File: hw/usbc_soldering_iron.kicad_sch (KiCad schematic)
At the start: 78 parts, among them J1 USB_C_Receptacle_USB2.0_14P, J10 TIP_L, J11 TIP_H, J12 TIP_K, J13 TIP_L, J14 TIP_H, J15 TIP_K, J16 TIP_L, J2 DBG, J3 LED RING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

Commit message: mosfets and driver
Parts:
- added C29, C30, C31: 100n, Capacitor_SMD:C_0603_1608Metric, symbol Device:C_Small
- added D1: CDBU40-HF, Diode_SMD:D_0603_1608Metric, symbol Diode:CDBU40-HF
- added Q1, Q2: CSD16327Q3, Package_SON:VSON-8_3.3x3.3mm_P0.65mm_NexFET, symbol Transistor_FET:CSD16327Q3
- added R10: 1.5m, Resistor_SMD:R_1206_3216Metric, symbol Device:R_Small
- added R11: 10k, Capacitor_SMD:C_0603_1608Metric, symbol Device:R_Small
- added U10: PLM74502QDDFRQ1, Package_TO_SOT_SMD:SOT-23-8, symbol custom_library:PLM74502QDDFRQ1
- added U8: IRS20752L, Package_TO_SOT_SMD:SOT-23-6, symbol custom_library:IRS20752L
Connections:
- net +3.3V: now also C30.1, D1.2 (A), U8.1 (VCC)
- net GND: now also C30.2, U10.2 (GND), U8.2 (COM)
- net HEATER_ON: now also U8.3 (IN)
- net VBUS: now also U6.4 (IN+), R10.1; no longer C23.1, C25.1, L2.1
- net at U6.5 (IN-): now also C31.1, Q2.5 (D), R10.2, R11.1, U10.5 (VS)
- net at C26.1, C28.1, L2.2: now also Q1.5 (D)
- new net: C31.2, U10.4 (VCAP)
- new net: Q2.4 (G), U10.6 (GATE)
- new net: C23.1, C25.1, L2.1, Q2.1 (S), Q2.2 (S), Q2.3 (S), R11.2, U10.8 (SRC)
- new net: C29.1, D1.1 (K), U8.6 (VB)
- new net: C29.2, Q1.1 (S), Q1.2 (S), Q1.3 (S), U8.4 (VS)
- new net: Q1.4 (G), U8.5 (HO)
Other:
- note removed: "TIP CONTROL"
- moved on the sheet: C14, C23, C25, C26, C28, L2, U6

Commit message: different mosfets
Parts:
- removed C31: 100n, Capacitor_SMD:C_0603_1608Metric, symbol Device:C_Small
- removed Q2: CSD16327Q3, Package_SON:VSON-8_3.3x3.3mm_P0.65mm_NexFET, symbol Transistor_FET:CSD16327Q3
- removed R11: 10k, Capacitor_SMD:C_0603_1608Metric, symbol Device:R_Small
- removed U10: PLM74502QDDFRQ1, Package_TO_SOT_SMD:SOT-23-8, symbol custom_library:PLM74502QDDFRQ1
- added U10: CSD25402Q3A, Package_SON:VSON-8_3.3x3.3mm_P0.65mm_NexFET, symbol Transistor_FET:CSD25402Q3A
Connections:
- net at R10.2, U6.5 (IN-): now also U10.5 (S)
- net at C23.1, C25.1, L2.1: now also U10.1 (D), U10.2 (D), U10.3 (D)

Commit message: work on model
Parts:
- added SW4: SW_Push, symbol Switch:SW_Push
- L1: footprint Inductor_SMD:L_Changjiang_FTC201607S -> Inductor_SMD:L_Changjiang_FTC252012S
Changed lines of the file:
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@@
 			)
 		)
-		(property "Footprint" "Inductor_SMD:L_Changjiang_FTC201607S"
+		(property "Footprint" "Inductor_SMD:L_Changjiang_FTC252012S"
 			(at 152.4 27.94 0)
 			(effects
@@
 					(unit 1)
 				)
+			)
+		)
+	)
+	(symbol
+		(lib_id "Switch:SW_Push")
+		(at 217.17 234.95 0)
+		(unit 1)
+		(exclude_from_sim no)
+		(in_bom yes)
+		(on_board yes)
+		(dnp no)
+		(fields_autoplaced yes)
+		(property "Reference" "SW4"
+			(at 217.17 227.33 0)
+			(effects
+				(font
+					(size 1.27 1.27)
+				)
+			)
+		)
+		(property "Value" "SW_Push"
+			(at 217.17 229.87 0)
+			(effects
+				(font
+					(size 1.27 1.27)
+				)
+			)
+		)
+		(property "Footprint" ""
+			(at 217.17 229.87 0)
+			(effects
+				(font
+					(size 1.27 1.27)
+				)
+				(hide yes)
+			)
+		)
+		(property "Datasheet" "~"
+			(at 217.17 229.87 0)
+			(effects
+				(font
+					(size 1.27 1.27)
+				)
+				(hide yes)
+			)
+		)
+		(property "Description" "Push button switch, generic, two pins"
+			(at 217.17 234.95 0)
+			(effects
+				(font
+					(size 1.27 1.27)
+				)
+				(hide yes)
+			)
+		)
+		(pin "2"
+		)
+		(pin "1"
+		)
+		(instances
+			(project ""
+				(path "/7095b018-eac3-4b01-b374-28e3216c4fd8"
+					(reference "SW4")
+					(unit 1)
+				)

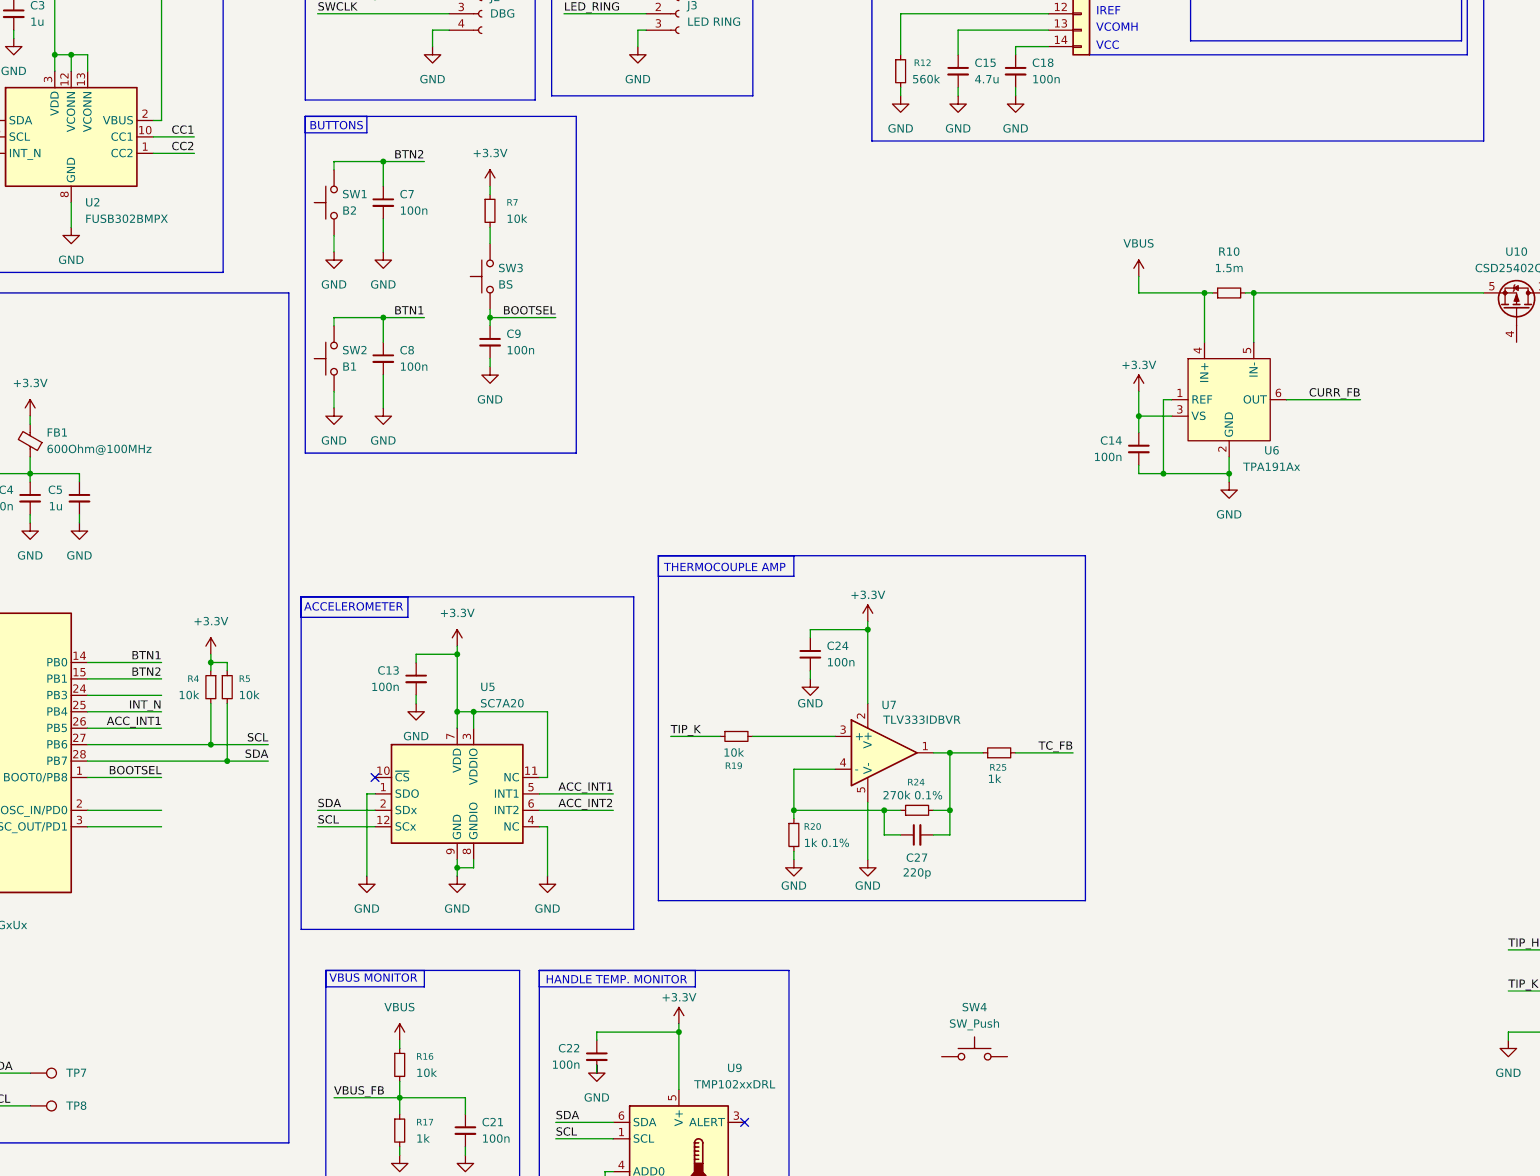
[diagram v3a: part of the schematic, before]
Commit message: rotary encoder and model for usb receptacle
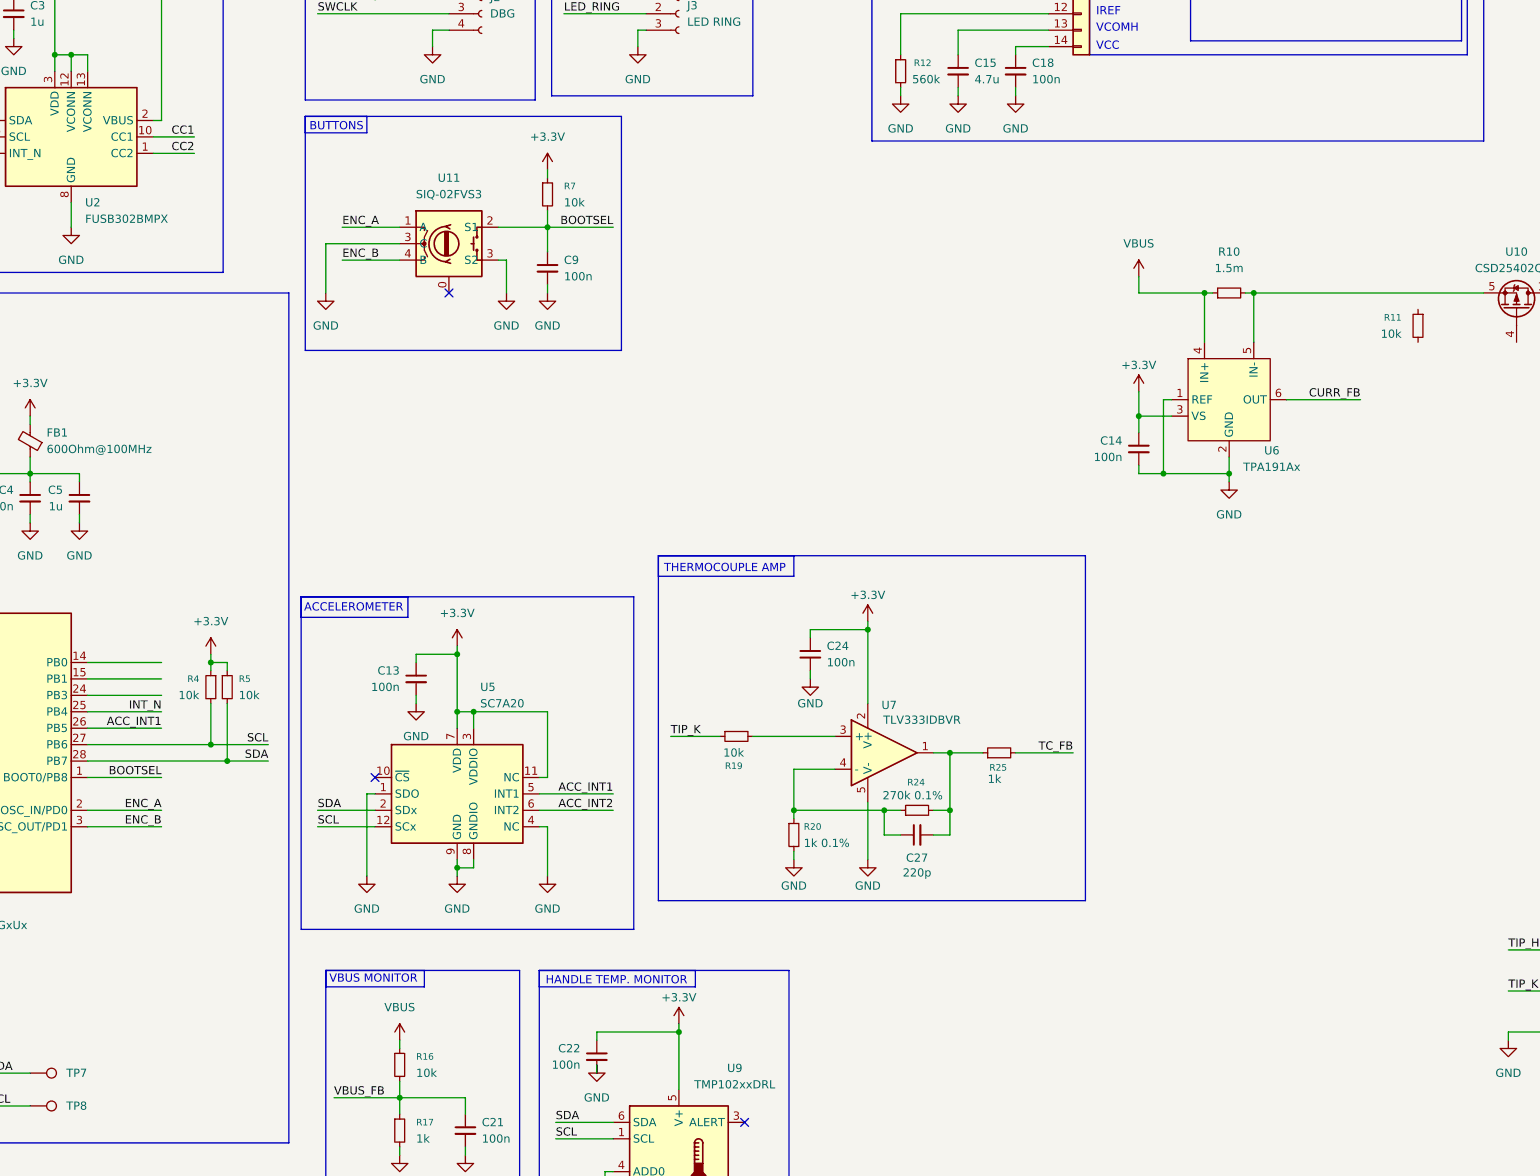
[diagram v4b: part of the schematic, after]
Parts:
- removed C7, C8: 100n, Capacitor_SMD:C_0603_1608Metric, symbol Device:C_Small
- removed SW1: B2, Button_Switch_SMD:SW_SPST_TS-1088-xR020, symbol Switch:SW_Push
- removed SW2: B1, Button_Switch_SMD:SW_SPST_TS-1088-xR020, symbol Switch:SW_Push
- removed SW3: BS, Button_Switch_SMD:SW_SPST_TS-1088-xR020, symbol Switch:SW_Push
- removed SW4: SW_Push, symbol Switch:SW_Push
- added R11: 10k, Resistor_SMD:R_0603_1608Metric, symbol Device:R_Small
- added U11: SIQ-02FVS3, Custom:SIQ-02FVS3_Rotary_Encoder, symbol custom_library:SIQ-02FVS#
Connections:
- net BOOTSEL: now also R7.2, U11.2 (S1)
- net GND: now also U11.3 (S2)
- net ENC_A: now reaches U1.2 (OSC_IN/PD0)
- net ENC_A: now also U11.1 (A)
- net ENC_B: now reaches U1.3 (OSC_OUT/PD1)
- net ENC_B: now also U11.4 (B)
- net BTN1: no longer names the net of U1.14 (PB0)
- net BTN2: no longer names the net of U1.15 (PB1)
- no-connect marks 7 -> 8
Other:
- moved on the sheet: C9, R7

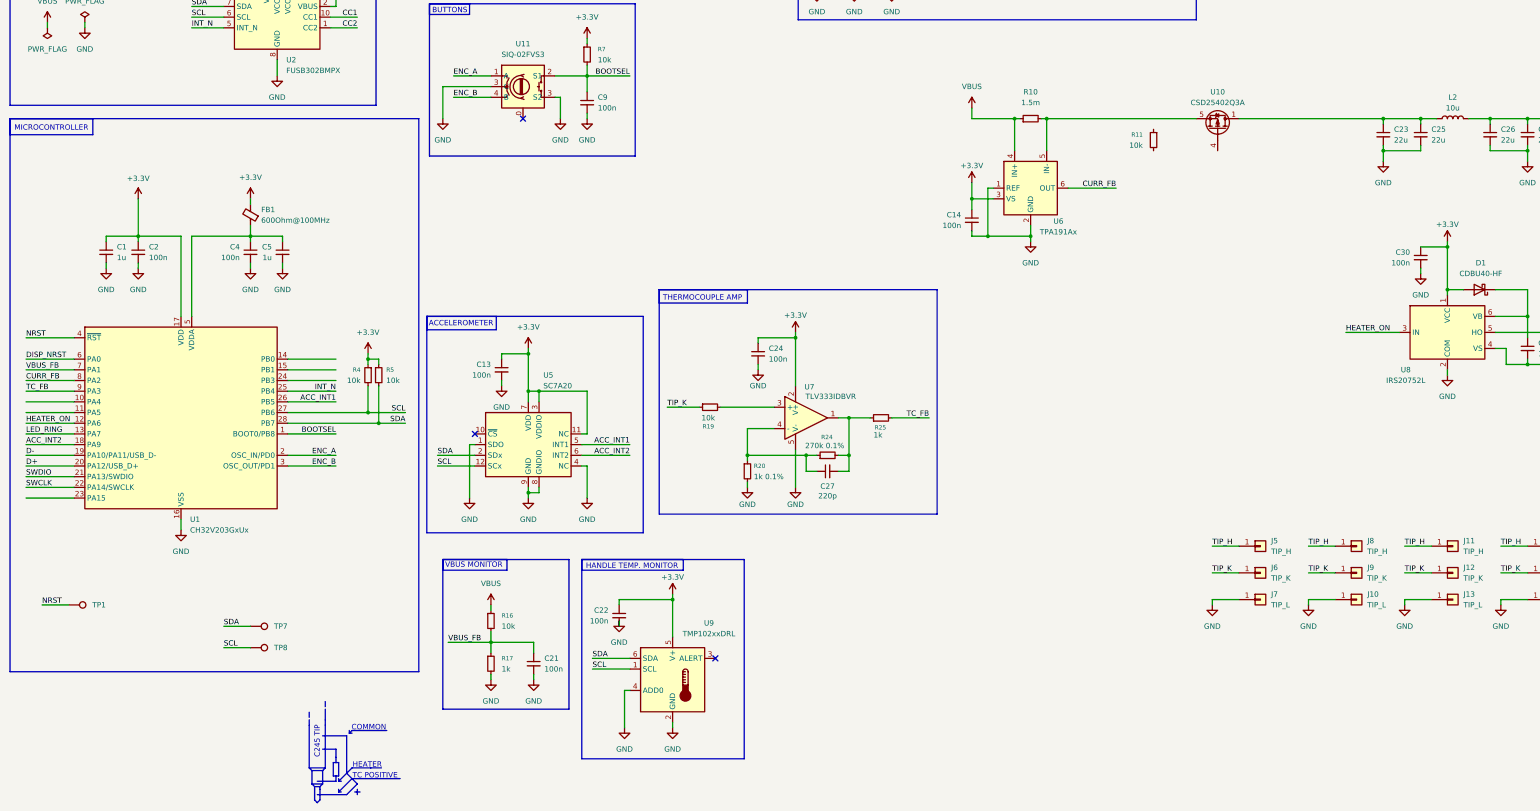
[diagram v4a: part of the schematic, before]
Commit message: changed power stage and monitoring ICs
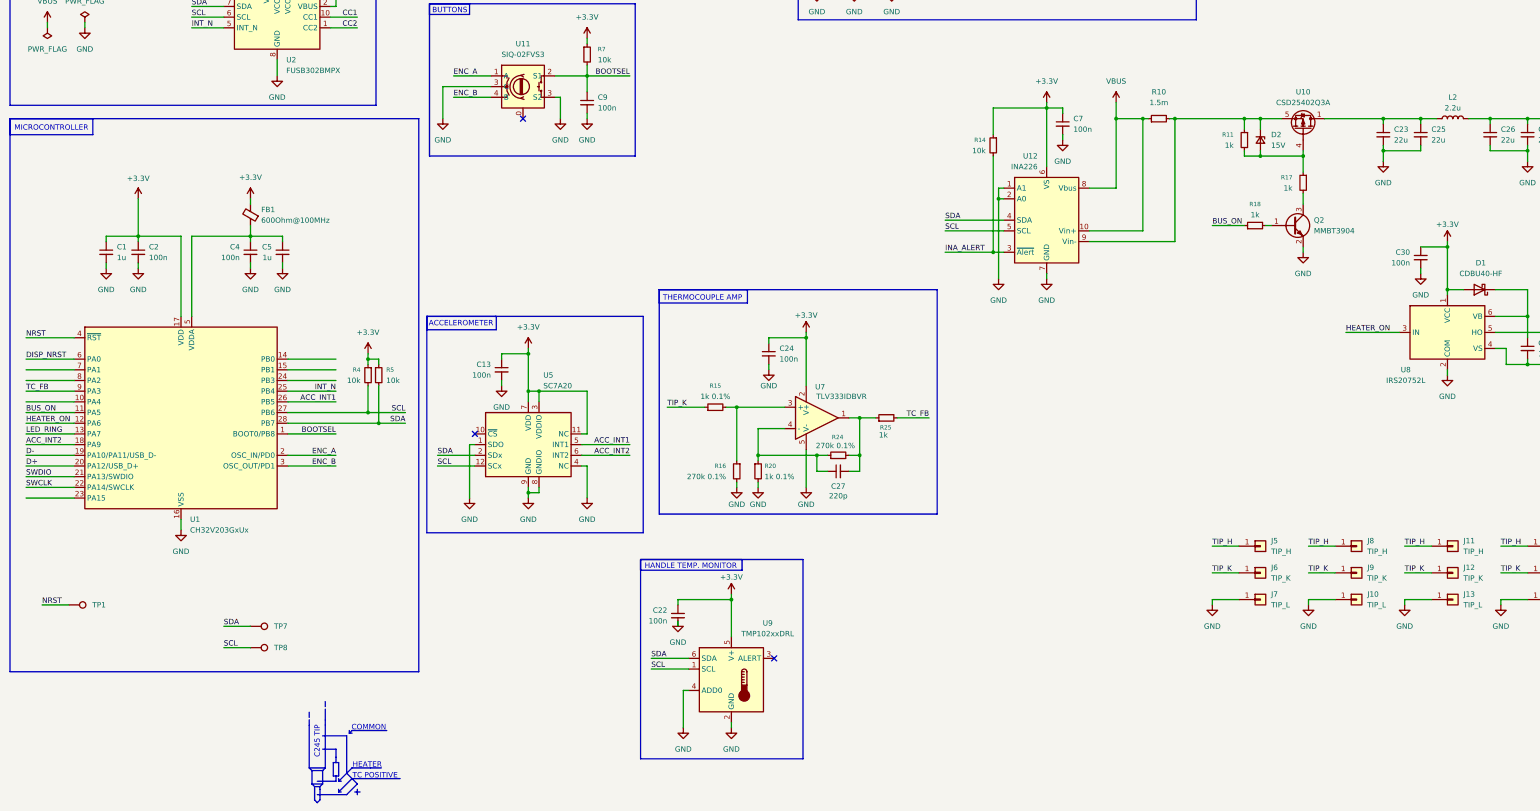
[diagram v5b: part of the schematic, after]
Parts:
- removed C14, C21: 100n, Capacitor_SMD:C_0603_1608Metric, symbol Device:C_Small
- removed R19: 10k, Resistor_SMD:R_0603_1608Metric, symbol Device:R_Small
- removed U6: TPA191Ax, Package_TO_SOT_SMD:SOT-363_SC-70-6, symbol custom_library:TPA191Ax
- added C7: 100n, Capacitor_SMD:C_0603_1608Metric, symbol Device:C_Small
- added D2: 15V, Diode_SMD:D_SOD-323, symbol Device:D_Zener_Small
- added Q2: MMBT3904, Package_TO_SOT_SMD:SOT-23, symbol Transistor_BJT:MMBT3904
- added R14: 10k, Resistor_SMD:R_0603_1608Metric, symbol Device:R_Small
- added R15: 1k 0.1%, Resistor_SMD:R_0603_1608Metric, symbol Device:R_Small
- added R18: 1k, Resistor_SMD:R_0603_1608Metric, symbol Device:R_Small
- added U12: INA226, Package_SO:VSSOP-10_3x3mm_P0.5mm, symbol Sensor_Energy:INA226
- L2: value 10u -> 2.2u; footprint Inductor_SMD:L_Coilcraft_XAL6060-XXX -> Inductor_SMD:L_Changjiang_FTC404030S
- R11: value 10k -> 1k
- R16: value 10k -> 270k 0.1%
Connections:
- net +3.3V: now also C7.1, R14.1, U12.6 (VS)
- net GND: now also R16.2, C7.2, Q2.2 (E), U12.1 (A1), U12.2 (A0), U12.7 (GND); no longer R17.2
- net SCL: now also U12.5 (SCL)
- net SDA: now also U12.4 (SDA)
- net TIP_K: now also R15.1
- net VBUS: now also U12.10 (Vin+), U12.8 (Vbus); no longer R16.1
- net at U7.3 (+): now also R16.1, R15.2
- net BUS_ON: now reaches U1.11 (PA5)
- net BUS_ON: now also R18.1
- net at R10.2, U10.5 (S): now also R11.1, D2.1 (K), U12.9 (Vin-)
- net at R11.2: now also R17.1, U10.4 (G), D2.2 (A)
- net CURR_FB: no longer names the net of U1.8 (PA2)
- removed net VBUS_FB: R16.2, R17.1, U1.7 (PA1)
- new net: Q2.1 (B), R18.2
- new net: Q2.3 (C), R17.2
- new net INA_ALERT: R14.2, U12.3 (~{Alert})
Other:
- note removed: "VBUS MONITOR"
- moved on the sheet: C22, C24, C27, R10, R11, R20, R24, R25, U10, U7, U9
